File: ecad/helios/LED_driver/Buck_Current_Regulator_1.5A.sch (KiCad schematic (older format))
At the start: 21 parts, among them U2 TPS92512

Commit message: Finishes the schematics
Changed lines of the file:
@@
 AR Path="/5AA2AB58/5AA2AC23" Ref="U2"  Part="1"
 AR Path="/5AA6DCFC/5AA2AC23" Ref="U3"  Part="1"
-F 0 "U2" H 6100 3150 60  0000 C CNN
+F 0 "U3" H 6100 3150 60  0000 C CNN
 F 1 "TPS92512" H 6250 2000 60  0000 C CNN
 F 2 "FORT:PDSO-10-1EP-3x3mm-Pitch0.5mm" H 6150 2550 60  0001 C CNN
@@
 AR Path="/5AA2AB58/5AA7001C" Ref="C8"  Part="1"
 AR Path="/5AA6DCFC/5AA7001C" Ref="C18"  Part="1"
-F 0 "C8" H 2125 2650 50  0000 L CNN
+F 0 "C18" H 2125 2650 50  0000 L CNN
 F 1 "4.7uF,50V" H 2125 2450 50  0000 L CNN
 F 2 "Capacitors_SMD:C_1206" H 2138 2400 50  0001 C CNN
@@
 AR Path="/5AA2AB58/5AA2B956" Ref="L1"  Part="1"
 AR Path="/5AA6DCFC/5AA2B956" Ref="L2"  Part="1"
-F 0 "L1" V 8100 2250 50  0000 C CNN
+F 0 "L2" V 8100 2250 50  0000 C CNN
 F 1 "100uH, 2.5A" V 7950 2250 50  0000 C CNN
 F 2 "Inductors_SMD:L_Wuerth_WE-PD-Typ-LS" H 8000 2250 50  0001 C CNN
@@
 AR Path="/5AA2AB58/5AA7001E" Ref="D2"  Part="1"
 AR Path="/5AA6DCFC/5AA7001E" Ref="D4"  Part="1"
-F 0 "D2" H 7800 2800 50  0000 C CNN
+F 0 "D4" H 7800 2800 50  0000 C CNN
 F 1 "60V, 2A" H 7800 2600 50  0000 C CNN
 F 2 "Diodes_SMD:D_SMB" H 7800 2700 50  0001 C CNN
@@
 AR Path="/5AA2AB58/5AA7001F" Ref="D1"  Part="1"
 AR Path="/5AA6DCFC/5AA7001F" Ref="D3"  Part="1"
-F 0 "D1" H 7100 1700 50  0000 C CNN
+F 0 "D3" H 7100 1700 50  0000 C CNN
 F 1 "60V, 2A" H 7100 1500 50  0000 C CNN
 F 2 "Diodes_SMD:D_SMB" H 7100 1600 50  0001 C CNN
@@
 $EndComp
 $Comp
-L GND #PWR015
+L GND #PWR016
 U 1 1 5AA70020
 P 8400 3750
-AR Path="/5AA2AB58/5AA70020" Ref="#PWR015"  Part="1"
-AR Path="/5AA6DCFC/5AA70020" Ref="#PWR017"  Part="1"
-F 0 "#PWR015" H 8400 3500 50  0001 C CNN
+AR Path="/5AA2AB58/5AA70020" Ref="#PWR016"  Part="1"
+AR Path="/5AA6DCFC/5AA70020" Ref="#PWR018"  Part="1"
+F 0 "#PWR018" H 8400 3500 50  0001 C CNN
 F 1 "GND" H 8400 3600 50  0000 C CNN
 F 2 "" H 8400 3750 50  0001 C CNN
@@
 AR Path="/5AA2AB58/5AA70021" Ref="R9"  Part="1"
 AR Path="/5AA6DCFC/5AA70021" Ref="R16"  Part="1"
-F 0 "R9" V 7280 2600 50  0000 C CNN
+F 0 "R16" V 7280 2600 50  0000 C CNN
 F 1 "1K" V 7200 2600 50  0000 C CNN
 F 2 "Resistors_SMD:R_0603" V 7130 2600 50  0001 C CNN
@@
 AR Path="/5AA2AB58/5AA70022" Ref="R13"  Part="1"
 AR Path="/5AA6DCFC/5AA70022" Ref="R20"  Part="1"
-F 0 "R13" V 8480 3350 50  0000 C CNN
+F 0 "R20" V 8480 3350 50  0000 C CNN
 F 1 "0.2, 1%, 0.5W" H 8700 3200 50  0000 C CNN
 F 2 "Resistors_SMD:R_1206" V 8330 3350 50  0001 C CNN
@@
 AR Path="/5AA2AB58/5AA70023" Ref="R8"  Part="1"
 AR Path="/5AA6DCFC/5AA70023" Ref="R15"  Part="1"
-F 0 "R8" V 5580 2250 50  0000 C CNN
+F 0 "R15" V 5580 2250 50  0000 C CNN
 F 1 "10M" V 5500 2250 50  0000 C CNN
 F 2 "Resistors_SMD:R_0603" V 5430 2250 50  0001 C CNN
@@
 AR Path="/5AA2AB58/5AA70024" Ref="R7"  Part="1"
 AR Path="/5AA6DCFC/5AA70024" Ref="R14"  Part="1"
-F 0 "R7" V 4530 2250 50  0000 C CNN
+F 0 "R14" V 4530 2250 50  0000 C CNN
 F 1 "1.96M" V 4450 2250 50  0000 C CNN
 F 2 "Resistors_SMD:R_0603" V 4380 2250 50  0001 C CNN
@@
 AR Path="/5AA2AB58/5AA70025" Ref="R10"  Part="1"
 AR Path="/5AA6DCFC/5AA70025" Ref="R17"  Part="1"
-F 0 "R10" V 4530 2750 50  0000 C CNN
+F 0 "R17" V 4530 2750 50  0000 C CNN
 F 1 "66.5k" V 4450 2750 50  0000 C CNN
 F 2 "Resistors_SMD:R_0603" V 4380 2750 50  0001 C CNN
@@
 AR Path="/5AA2AB58/5AA69587" Ref="R11"  Part="1"
 AR Path="/5AA6DCFC/5AA69587" Ref="R18"  Part="1"
-F 0 "R11" V 5430 3200 50  0000 C CNN
+F 0 "R18" V 5430 3200 50  0000 C CNN
 F 1 "267k" V 5350 3200 50  0000 C CNN
 F 2 "Resistors_SMD:R_0603" V 5280 3200 50  0001 C CNN
@@
 	5350 2950 5800 2950
 $Comp
-L GND #PWR016
+L GND #PWR017
 U 1 1 5AA69658
 P 5350 3500
-AR Path="/5AA2AB58/5AA69658" Ref="#PWR016"  Part="1"
-AR Path="/5AA6DCFC/5AA69658" Ref="#PWR018"  Part="1"
-F 0 "#PWR016" H 5350 3250 50  0001 C CNN
+AR Path="/5AA2AB58/5AA69658" Ref="#PWR017"  Part="1"
+AR Path="/5AA6DCFC/5AA69658" Ref="#PWR019"  Part="1"
+F 0 "#PWR019" H 5350 3250 50  0001 C CNN
 F 1 "GND" H 5350 3350 50  0000 C CNN
 F 2 "" H 5350 3500 50  0001 C CNN
@@
 AR Path="/5AA2AB58/5AA696F3" Ref="R12"  Part="1"
 AR Path="/5AA6DCFC/5AA696F3" Ref="R19"  Part="1"
-F 0 "R12" V 5780 3200 50  0000 C CNN
+F 0 "R19" V 5780 3200 50  0000 C CNN
 F 1 "4.02k" V 5700 3200 50  0000 C CNN
 F 2 "Resistors_SMD:R_0603" V 5630 3200 50  0001 C CNN
@@
 AR Path="/5AA2AB58/5AA69900" Ref="C15"  Part="1"
 AR Path="/5AA6DCFC/5AA69900" Ref="C25"  Part="1"
-F 0 "C15" H 5725 3750 50  0000 L CNN
+F 0 "C25" H 5725 3750 50  0000 L CNN
 F 1 "470pF" H 5725 3550 50  0000 L CNN
 F 2 "Capacitors_SMD:C_0603" H 5738 3500 50  0001 C CNN
@@
 AR Path="/5AA2AB58/5AA69C44" Ref="C11"  Part="1"
 AR Path="/5AA6DCFC/5AA69C44" Ref="C21"  Part="1"
-F 0 "C11" H 3675 2650 50  0000 L CNN
+F 0 "C21" H 3675 2650 50  0000 L CNN
 F 1 "10nF, 50V" H 3675 2450 50  0000 L CNN
 F 2 "Capacitors_SMD:C_0603" H 3688 2400 50  0001 C CNN
@@
 AR Path="/5AA2AB58/5AA7002B" Ref="C14"  Part="1"
 AR Path="/5AA6DCFC/5AA7002B" Ref="C24"  Part="1"
-F 0 "C14" H 4875 3200 50  0000 L CNN
+F 0 "C24" H 4875 3200 50  0000 L CNN
 F 1 "100nF" H 4875 3000 50  0000 L CNN
 F 2 "Capacitors_SMD:C_0603" H 4888 2950 50  0001 C CNN
@@
 AR Path="/5AA2AB58/5AA6A967" Ref="C9"  Part="1"
 AR Path="/5AA6DCFC/5AA6A967" Ref="C19"  Part="1"
-F 0 "C9" H 2675 2650 50  0000 L CNN
+F 0 "C19" H 2675 2650 50  0000 L CNN
 F 1 "4.7uF,50V" H 2675 2450 50  0000 L CNN
 F 2 "Capacitors_SMD:C_1206" H 2688 2400 50  0001 C CNN
@@
 AR Path="/5AA2AB58/5AA6A9D1" Ref="C10"  Part="1"
 AR Path="/5AA6DCFC/5AA6A9D1" Ref="C20"  Part="1"
-F 0 "C10" H 3175 2650 50  0000 L CNN
+F 0 "C20" H 3175 2650 50  0000 L CNN
 F 1 "4.7uF,50V" H 3175 2450 50  0000 L CNN
 F 2 "Capacitors_SMD:C_1206" H 3188 2400 50  0001 C CNN
@@
 AR Path="/5AA2AB58/5AA7002E" Ref="C6"  Part="1"
 AR Path="/5AA6DCFC/5AA7002E" Ref="C16"  Part="1"
-F 0 "C6" V 7350 2150 50  0000 L CNN
+F 0 "C16" V 7350 2150 50  0000 L CNN
 F 1 "100nF" V 7100 1950 50  0000 L CNN
 F 2 "Capacitors_SMD:C_0603" H 7288 1900 50  0001 C CNN
@@
 AR Path="/5AA2AB58/5AA6B735" Ref="C12"  Part="1"
 AR Path="/5AA6DCFC/5AA6B735" Ref="C22"  Part="1"
-F 0 "C12" H 8425 2750 50  0000 L CNN
+F 0 "C22" H 8425 2750 50  0000 L CNN
 F 1 "4.7uF,50V" H 8425 2550 50  0000 L CNN
 F 2 "Capacitors_SMD:C_1206" H 8438 2500 50  0001 C CNN
@@
 AR Path="/5AA2AB58/5AAA9295" Ref="C7"  Part="1"
 AR Path="/5AA6DCFC/5AAA9295" Ref="C17"  Part="1"
-F 0 "C7" H 1775 2650 50  0000 L CNN
+F 0 "C17" H 1775 2650 50  0000 L CNN
 F 1 "4.7uF,50V" H 1775 2450 50  0000 L CNN
 F 2 "Capacitors_SMD:C_1206" H 1788 2400 50  0001 C CNN
@@
 AR Path="/5AA2AB58/5AAA9C17" Ref="C13"  Part="1"
 AR Path="/5AA6DCFC/5AAA9C17" Ref="C23"  Part="1"
-F 0 "C13" H 8975 2750 50  0000 L CNN
+F 0 "C23" H 8975 2750 50  0000 L CNN
 F 1 "4.7uF,50V" H 8975 2550 50  0000 L CNN
 F 2 "Capacitors_SMD:C_1206" H 8988 2500 50  0001 C CNN

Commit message: layouted the board
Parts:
- removed C15: 470pF, Capacitors_SMD:C_0603, symbol C
- removed R12: 4.02k, Resistors_SMD:R_0603, symbol R
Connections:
- net PHI: now reaches C6.1, D2.1 (K), L1.1, U2.10 (PH)
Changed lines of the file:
@@
 Wire Wire Line
 	5350 3500 5350 3350
-$Comp
-L R R12
-U 1 1 5AA696F3
-P 5700 3200
-AR Path="/5AA2AB58/5AA696F3" Ref="R12"  Part="1"
-AR Path="/5AA6DCFC/5AA696F3" Ref="R19"  Part="1"
-F 0 "R19" V 5780 3200 50  0000 C CNN
-F 1 "4.02k" V 5700 3200 50  0000 C CNN
-F 2 "Resistors_SMD:R_0603" V 5630 3200 50  0001 C CNN
-F 3 "" H 5700 3200 50  0001 C CNN
-F 4 "RMCF0603FT4K02" H 5700 3200 60  0001 C CNN "Part Number"
-	1    5700 3200
-	1    0    0    -1
-$EndComp
 Wire Wire Line
 	4450 2900 4450 3400
@@
 	1750 3400 5350 3400
 Connection ~ 5350 3400
-$Comp
-L C C15
-U 1 1 5AA69900
-P 5700 3650
-AR Path="/5AA2AB58/5AA69900" Ref="C15"  Part="1"
-AR Path="/5AA6DCFC/5AA69900" Ref="C25"  Part="1"
-F 0 "C25" H 5725 3750 50  0000 L CNN
-F 1 "470pF" H 5725 3550 50  0000 L CNN
-F 2 "Capacitors_SMD:C_0603" H 5738 3500 50  0001 C CNN
-F 3 "" H 5700 3650 50  0001 C CNN
-F 4 "06035C471KAT2A" H 5700 3650 60  0001 C CNN "Part Number"
-	1    5700 3650
-	1    0    0    -1
-$EndComp
-Wire Wire Line
-	5700 3050 5700 2950
-Connection ~ 5700 2950
-Wire Wire Line
-	5700 3350 5700 3500
-Wire Wire Line
-	5700 3800 5700 3900
-Wire Wire Line
-	5700 3900 5300 3900
-Text HLabel 5300 3900 0    60   Input ~ 0
-SYNC
 $Comp
 L C C11
@@
 	8950 2500 8950 2250
 Connection ~ 8950 2250
+Text Label 7050 2250 0    60   ~ 0
+PHI
 $EndSCHEMATC

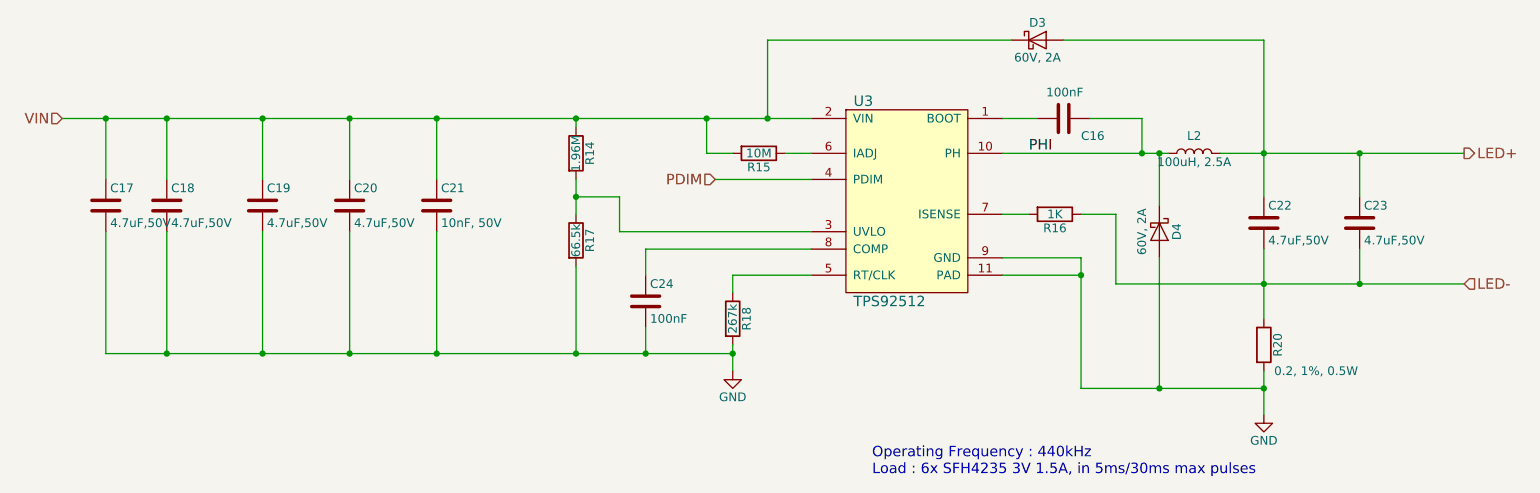
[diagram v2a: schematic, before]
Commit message: Fixes small mistakes on the PCB
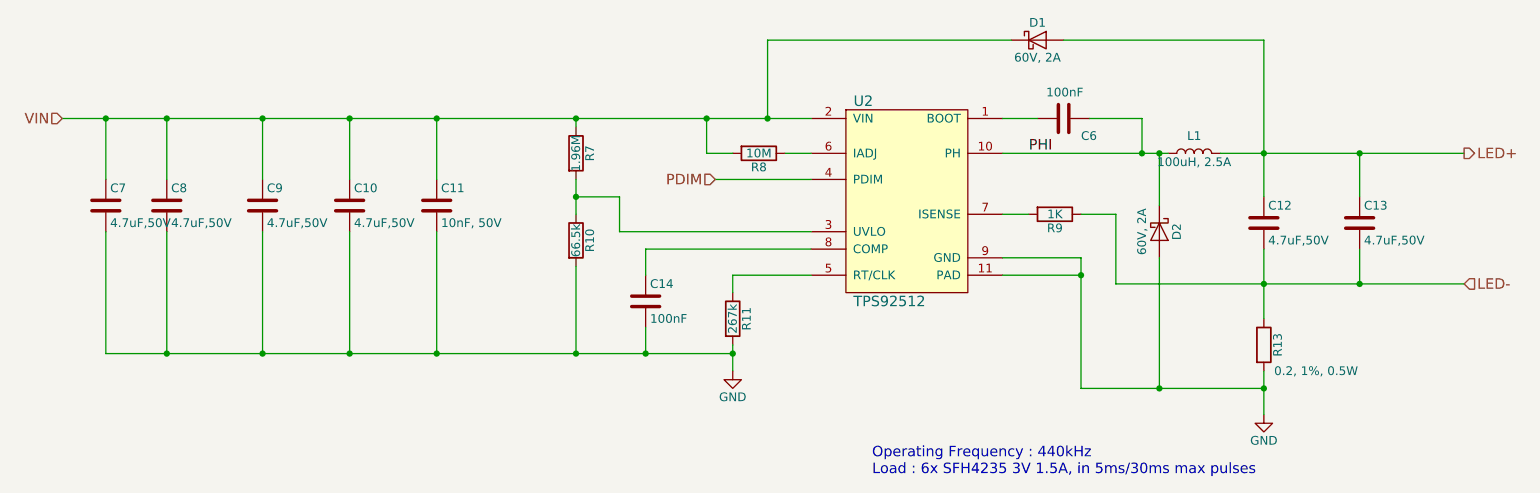
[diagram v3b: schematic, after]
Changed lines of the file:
@@
 AR Path="/5AA2AB58/5AA2AC23" Ref="U2"  Part="1"
 AR Path="/5AA6DCFC/5AA2AC23" Ref="U3"  Part="1"
-F 0 "U3" H 6100 3150 60  0000 C CNN
+F 0 "U2" H 6100 3150 60  0000 C CNN
 F 1 "TPS92512" H 6250 2000 60  0000 C CNN
 F 2 "FORT:PDSO-10-1EP-3x3mm-Pitch0.5mm" H 6150 2550 60  0001 C CNN
@@
 AR Path="/5AA2AB58/5AA7001C" Ref="C8"  Part="1"
 AR Path="/5AA6DCFC/5AA7001C" Ref="C18"  Part="1"
-F 0 "C18" H 2125 2650 50  0000 L CNN
+F 0 "C8" H 2125 2650 50  0000 L CNN
 F 1 "4.7uF,50V" H 2125 2450 50  0000 L CNN
 F 2 "Capacitors_SMD:C_1206" H 2138 2400 50  0001 C CNN
@@
 AR Path="/5AA2AB58/5AA2B956" Ref="L1"  Part="1"
 AR Path="/5AA6DCFC/5AA2B956" Ref="L2"  Part="1"
-F 0 "L2" V 8100 2250 50  0000 C CNN
+F 0 "L1" V 8100 2250 50  0000 C CNN
 F 1 "100uH, 2.5A" V 7950 2250 50  0000 C CNN
 F 2 "Inductors_SMD:L_Wuerth_WE-PD-Typ-LS" H 8000 2250 50  0001 C CNN
@@
 AR Path="/5AA2AB58/5AA7001E" Ref="D2"  Part="1"
 AR Path="/5AA6DCFC/5AA7001E" Ref="D4"  Part="1"
-F 0 "D4" H 7800 2800 50  0000 C CNN
+F 0 "D2" H 7800 2800 50  0000 C CNN
 F 1 "60V, 2A" H 7800 2600 50  0000 C CNN
 F 2 "Diodes_SMD:D_SMB" H 7800 2700 50  0001 C CNN
@@
 AR Path="/5AA2AB58/5AA7001F" Ref="D1"  Part="1"
 AR Path="/5AA6DCFC/5AA7001F" Ref="D3"  Part="1"
-F 0 "D3" H 7100 1700 50  0000 C CNN
+F 0 "D1" H 7100 1700 50  0000 C CNN
 F 1 "60V, 2A" H 7100 1500 50  0000 C CNN
 F 2 "Diodes_SMD:D_SMB" H 7100 1600 50  0001 C CNN
@@
 AR Path="/5AA2AB58/5AA70020" Ref="#PWR016"  Part="1"
 AR Path="/5AA6DCFC/5AA70020" Ref="#PWR018"  Part="1"
-F 0 "#PWR018" H 8400 3500 50  0001 C CNN
+F 0 "#PWR016" H 8400 3500 50  0001 C CNN
 F 1 "GND" H 8400 3600 50  0000 C CNN
 F 2 "" H 8400 3750 50  0001 C CNN
@@
 AR Path="/5AA2AB58/5AA70021" Ref="R9"  Part="1"
 AR Path="/5AA6DCFC/5AA70021" Ref="R16"  Part="1"
-F 0 "R16" V 7280 2600 50  0000 C CNN
+F 0 "R9" V 7280 2600 50  0000 C CNN
 F 1 "1K" V 7200 2600 50  0000 C CNN
 F 2 "Resistors_SMD:R_0603" V 7130 2600 50  0001 C CNN
@@
 AR Path="/5AA2AB58/5AA70022" Ref="R13"  Part="1"
 AR Path="/5AA6DCFC/5AA70022" Ref="R20"  Part="1"
-F 0 "R20" V 8480 3350 50  0000 C CNN
+F 0 "R13" V 8480 3350 50  0000 C CNN
 F 1 "0.2, 1%, 0.5W" H 8700 3200 50  0000 C CNN
 F 2 "Resistors_SMD:R_1206" V 8330 3350 50  0001 C CNN
@@
 AR Path="/5AA2AB58/5AA70023" Ref="R8"  Part="1"
 AR Path="/5AA6DCFC/5AA70023" Ref="R15"  Part="1"
-F 0 "R15" V 5580 2250 50  0000 C CNN
+F 0 "R8" V 5580 2250 50  0000 C CNN
 F 1 "10M" V 5500 2250 50  0000 C CNN
 F 2 "Resistors_SMD:R_0603" V 5430 2250 50  0001 C CNN
@@
 AR Path="/5AA2AB58/5AA70024" Ref="R7"  Part="1"
 AR Path="/5AA6DCFC/5AA70024" Ref="R14"  Part="1"
-F 0 "R14" V 4530 2250 50  0000 C CNN
+F 0 "R7" V 4530 2250 50  0000 C CNN
 F 1 "1.96M" V 4450 2250 50  0000 C CNN
 F 2 "Resistors_SMD:R_0603" V 4380 2250 50  0001 C CNN
@@
 AR Path="/5AA2AB58/5AA70025" Ref="R10"  Part="1"
 AR Path="/5AA6DCFC/5AA70025" Ref="R17"  Part="1"
-F 0 "R17" V 4530 2750 50  0000 C CNN
+F 0 "R10" V 4530 2750 50  0000 C CNN
 F 1 "66.5k" V 4450 2750 50  0000 C CNN
 F 2 "Resistors_SMD:R_0603" V 4380 2750 50  0001 C CNN
@@
 AR Path="/5AA2AB58/5AA69587" Ref="R11"  Part="1"
 AR Path="/5AA6DCFC/5AA69587" Ref="R18"  Part="1"
-F 0 "R18" V 5430 3200 50  0000 C CNN
+F 0 "R11" V 5430 3200 50  0000 C CNN
 F 1 "267k" V 5350 3200 50  0000 C CNN
 F 2 "Resistors_SMD:R_0603" V 5280 3200 50  0001 C CNN
@@
 AR Path="/5AA2AB58/5AA69658" Ref="#PWR017"  Part="1"
 AR Path="/5AA6DCFC/5AA69658" Ref="#PWR019"  Part="1"
-F 0 "#PWR019" H 5350 3250 50  0001 C CNN
+F 0 "#PWR017" H 5350 3250 50  0001 C CNN
 F 1 "GND" H 5350 3350 50  0000 C CNN
 F 2 "" H 5350 3500 50  0001 C CNN
@@
 AR Path="/5AA2AB58/5AA69C44" Ref="C11"  Part="1"
 AR Path="/5AA6DCFC/5AA69C44" Ref="C21"  Part="1"
-F 0 "C21" H 3675 2650 50  0000 L CNN
+F 0 "C11" H 3675 2650 50  0000 L CNN
 F 1 "10nF, 50V" H 3675 2450 50  0000 L CNN
 F 2 "Capacitors_SMD:C_0603" H 3688 2400 50  0001 C CNN
@@
 AR Path="/5AA2AB58/5AA7002B" Ref="C14"  Part="1"
 AR Path="/5AA6DCFC/5AA7002B" Ref="C24"  Part="1"
-F 0 "C24" H 4875 3200 50  0000 L CNN
+F 0 "C14" H 4875 3200 50  0000 L CNN
 F 1 "100nF" H 4875 3000 50  0000 L CNN
 F 2 "Capacitors_SMD:C_0603" H 4888 2950 50  0001 C CNN
@@
 AR Path="/5AA2AB58/5AA6A967" Ref="C9"  Part="1"
 AR Path="/5AA6DCFC/5AA6A967" Ref="C19"  Part="1"
-F 0 "C19" H 2675 2650 50  0000 L CNN
+F 0 "C9" H 2675 2650 50  0000 L CNN
 F 1 "4.7uF,50V" H 2675 2450 50  0000 L CNN
 F 2 "Capacitors_SMD:C_1206" H 2688 2400 50  0001 C CNN
@@
 AR Path="/5AA2AB58/5AA6A9D1" Ref="C10"  Part="1"
 AR Path="/5AA6DCFC/5AA6A9D1" Ref="C20"  Part="1"
-F 0 "C20" H 3175 2650 50  0000 L CNN
+F 0 "C10" H 3175 2650 50  0000 L CNN
 F 1 "4.7uF,50V" H 3175 2450 50  0000 L CNN
 F 2 "Capacitors_SMD:C_1206" H 3188 2400 50  0001 C CNN
@@
 AR Path="/5AA2AB58/5AA7002E" Ref="C6"  Part="1"
 AR Path="/5AA6DCFC/5AA7002E" Ref="C16"  Part="1"
-F 0 "C16" V 7350 2150 50  0000 L CNN
+F 0 "C6" V 7350 2150 50  0000 L CNN
 F 1 "100nF" V 7100 1950 50  0000 L CNN
 F 2 "Capacitors_SMD:C_0603" H 7288 1900 50  0001 C CNN
@@
 AR Path="/5AA2AB58/5AA6B735" Ref="C12"  Part="1"
 AR Path="/5AA6DCFC/5AA6B735" Ref="C22"  Part="1"
-F 0 "C22" H 8425 2750 50  0000 L CNN
+F 0 "C12" H 8425 2750 50  0000 L CNN
 F 1 "4.7uF,50V" H 8425 2550 50  0000 L CNN
 F 2 "Capacitors_SMD:C_1206" H 8438 2500 50  0001 C CNN
@@
 AR Path="/5AA2AB58/5AAA9295" Ref="C7"  Part="1"
 AR Path="/5AA6DCFC/5AAA9295" Ref="C17"  Part="1"
-F 0 "C17" H 1775 2650 50  0000 L CNN
+F 0 "C7" H 1775 2650 50  0000 L CNN
 F 1 "4.7uF,50V" H 1775 2450 50  0000 L CNN
 F 2 "Capacitors_SMD:C_1206" H 1788 2400 50  0001 C CNN
@@
 AR Path="/5AA2AB58/5AAA9C17" Ref="C13"  Part="1"
 AR Path="/5AA6DCFC/5AAA9C17" Ref="C23"  Part="1"
-F 0 "C23" H 8975 2750 50  0000 L CNN
+F 0 "C13" H 8975 2750 50  0000 L CNN
 F 1 "4.7uF,50V" H 8975 2550 50  0000 L CNN
 F 2 "Capacitors_SMD:C_1206" H 8988 2500 50  0001 C CNN
